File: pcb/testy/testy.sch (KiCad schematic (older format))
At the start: 74 parts, among them J1 Conn_01x02, J2 Conn_01x02, SW0:0 SW_Push, SW0:1 SW_Push, SW0:2 SW_Push, SW0:3 SW_Push, SW0:4 SW_Push, SW0:5 SW_Push, SW1:0 SW_Push, SW1:1 SW_Push, SW1:2 SW_Push, SW1:3 SW_Push, SW1:4 SW_Push, SW1:5 SW_Push, SW2:0 SW_Push, SW2:1 SW_Push, SW2:2 SW_Push, SW2:3 SW_Push, SW2:4 SW_Push, SW2:5 SW_Push, SW3:0 SW_Push, SW3:1 SW_Push, SW3:2 SW_Push, SW3:3 SW_Push, SW3:4 SW_Push, SW3:5 SW_Push, SW3:6 SW_Push, SW4:0 SW_Push, SW4:1 SW_Push, SW4:2 SW_Push, SW4:3 SW_Push, SW4:4 SW_Push, SW4:5 SW_Push, SW4:6 SW_Push, U1 ProMicro

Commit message: feat: attempt to make usb-c breakout board footprint
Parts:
- added H1: USB-C Breakout Board, footprints:usb-c-breakout, symbol Mechanical:MountingHole
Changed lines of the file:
@@
 Wire Wire Line
 	10000 4650 10250 4650
+$Comp
+L Mechanical:MountingHole H1
+U 1 1 5DCB9C3F
+P 1950 7200
+F 0 "H1" H 2050 7246 50  0000 L CNN
+F 1 "USB-C Breakout Board" H 2050 7155 50  0000 L CNN
+F 2 "footprints:usb-c-breakout" H 1950 7200 50  0001 C CNN
+F 3 "~" H 1950 7200 50  0001 C CNN
+	1    1950 7200
+	1    0    0    -1
+$EndComp
 $EndSCHEMATC

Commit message: feat: add OLED and iCSP to schematic
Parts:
- added JP1, JP2, JP3, JP4, JP5, JP6, JP7, JP8: JP2, symbol jp2:JP2
- added P1: OLED, symbol conn_01x04:CONN_01X04
- added P2: iCSP, symbol conn_01x06:CONN_01X06
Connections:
- net labels added: MISO, MOSI, SCK, SCL, SDA
- wire segments 107 -> 148
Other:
- note added: "FIXME add I2C resistors"
- note added: "FIXME add LED resistors"
- note added: "FIXME can I use PD3 pin for driving an LED?\nAlternatively, can I drive 3 LEDs with fewer than 3 pins?"
- note added: "Left hand side"
- note added: "Right hand side"

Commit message: fix: updates related to copying helix underglow
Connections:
- net labels added: LED
- no-connect marks 0 -> 2
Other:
- note added: "FIXME can I use PD3 pin for driving an LED? Yes! Helix does it.\nAlternatively, can I drive 3 LEDs with fewer than 3 pins? Yes, use WS2812\n"
- note added: "FIXME remove separate LEDs and copy helix method of driving LEDs\nHelix D3 pin config means PD3, not D3=PD0"
- note removed: "FIXME can I use PD3 pin for driving an LED?\nAlternatively, can I drive 3 LEDs with fewer than 3 pins?"
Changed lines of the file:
@@
 	1200 5200 1200 5650
 Text GLabel 1250 1900 0    50   Input ~ 0
-LED0
-Text GLabel 1250 3000 0    50   Input ~ 0
-LED1
-Text GLabel 2250 3000 2    50   Input ~ 0
-LED2
+LED
 Text GLabel 2250 4700 2    50   Input ~ 0
 LED0
@@
 SCL
 Text Notes 900  1400 0    50   ~ 0
-FIXME can I use PD3 pin for driving an LED?\nAlternatively, can I drive 3 LEDs with fewer than 3 pins?
+FIXME can I use PD3 pin for driving an LED? Yes! Helix does it.\nAlternatively, can I drive 3 LEDs with fewer than 3 pins? Yes, use WS2812\n
 $Comp
 L conn_01x04:CONN_01X04 P1
@@
 Text Notes 8900 6100 2    50   ~ 0
 FIXME add LED resistors
+NoConn ~ 2250 3000
+NoConn ~ 1250 3000
+Text Notes 2600 5050 0    50   ~ 0
+FIXME remove separate LEDs and copy helix method of driving LEDs\nHelix D3 pin config means PD3, not D3=PD0
 $EndSCHEMATC

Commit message: feat: move to new 5 col version
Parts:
- removed D0:5, D1:5, D2:5, D3:6, D4:0, D4:6: 1N4148, Diode_THT:D_DO-35_SOD27_P7.62mm_Horizontal, symbol Diode:1N4148
- removed H1: USB-C Breakout Board, footprints:usb-c-breakout, symbol Mechanical:MountingHole
- removed J1, J2: Conn_01x02, footprints:edge-connector, symbol Connector_Generic:Conn_01x02
- removed LED0: LED, footprints:LED_D3.0mm, symbol led:LED
- removed LED1, LED2: LED, LED_THT:LED_D3.0mm, symbol led:LED
- removed SW0:5, SW1:5, SW2:5, SW3:6, SW4:0, SW4:6: SW_Push, footprints:kailh-socket-and-choc-solder-reversible, symbol Switch:SW_Push
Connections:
- net labels removed: LED0, LED1, LED2
- wire segments 148 -> 119
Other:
- note added: "FIXME add WSxxxx LED strips\nHelix D3 pin config means PD3, not D3=PD0"
- note removed: "FIXME can I use PD3 pin for driving an LED? Yes! Helix does it.\nAlternatively, can I drive 3 LEDs with fewer than 3 pins? Yes, use WS2812\n"
- note removed: "FIXME remove separate LEDs and copy helix method of driving LEDs\nHelix D3 pin config means PD3, not D3=PD0"

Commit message: feat: lots done, still need more LEDs, the I2C resistors and finish the traces
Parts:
- added LED1: SK6812mini, footprints:ws2812-single, symbol sk6812mini:SK6812mini
- JP1: value JP2 -> L_GND; footprint (none) -> footprints:Jumper
- JP2: value JP2 -> L_VCC; footprint (none) -> footprints:Jumper
- JP3: value JP2 -> L_SCL; footprint (none) -> footprints:Jumper
- JP4: value JP2 -> L_SDA; footprint (none) -> footprints:Jumper
- JP5: value JP2 -> R_SDA; footprint (none) -> footprints:Jumper
- JP6: value JP2 -> R_SCL; footprint (none) -> footprints:Jumper
- JP7: value JP2 -> R_VCC; footprint (none) -> footprints:Jumper
- JP8: value JP2 -> R_GND; footprint (none) -> footprints:Jumper
- P1: footprint (none) -> footprints:oled_header_helix
- P2: footprint (none) -> footprints:PinHeader_1x06_P2.54mm_Vertical
- renumbered U1 to PM1
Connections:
- net GND: now also LED1.2 (GND)
- net LED: now also LED1.3 (DIN)
- net VCC: now also LED1.4 (VDD)
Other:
- note removed: "FIXME add LED resistors"
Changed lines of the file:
@@
 Row2
 $Comp
-L promicro:ProMicro U1
+L promicro:ProMicro PM1
 U 1 1 5DB7A2E7
 P 1750 2250
-F 0 "U1" H 1750 2847 60  0000 C CNN
+F 0 "PM1" H 1750 2847 60  0000 C CNN
 F 1 "ProMicro" H 1750 2741 60  0000 C CNN
 F 2 "footprints:Pro_Micro_ergotravel" H 1750 2250 60  0001 C CNN
@@
 U 1 1 5DCD19CA
 P 4050 5700
-F 0 "P1" H 3967 6065 50  0000 C CNN
+F 0 "P1" H 3967 6065 50  0001 C CNN
 F 1 "OLED" H 3967 5974 50  0000 C CNN
-F 2 "" H 4050 5700 50  0000 C CNN
+F 2 "footprints:oled_header_helix" H 4050 5700 50  0001 C CNN
 F 3 "" H 4050 5700 50  0000 C CNN
 	1    4050 5700
@@
 U 1 1 5DCEEF2E
 P 4950 5400
-F 0 "JP1" V 4837 5400 50  0000 C CNN
-F 1 "JP2" V 4845 5400 40  0001 C CNN
-F 2 "" H 4950 5400 60  0000 C CNN
+F 0 "JP1" V 4837 5400 50  0001 C CNN
+F 1 "L_GND" V 4845 5400 40  0000 C CNN
+F 2 "footprints:Jumper" H 4950 5400 60  0001 C CNN
 F 3 "" H 4950 5400 60  0000 C CNN
 	1    4950 5400
@@
 U 1 1 5DCF00CE
 P 4950 5600
-F 0 "JP2" V 4837 5600 50  0000 C CNN
-F 1 "JP2" V 4845 5600 40  0001 C CNN
-F 2 "" H 4950 5600 60  0000 C CNN
+F 0 "JP2" V 4837 5600 50  0001 C CNN
+F 1 "L_VCC" V 4845 5600 40  0000 C CNN
+F 2 "footprints:Jumper" H 4950 5600 60  0001 C CNN
 F 3 "" H 4950 5600 60  0000 C CNN
 	1    4950 5600
@@
 U 1 1 5DCF0797
 P 4950 6000
-F 0 "JP4" V 4837 6000 50  0000 C CNN
-F 1 "JP2" V 4845 6000 40  0001 C CNN
-F 2 "" H 4950 6000 60  0000 C CNN
+F 0 "JP4" V 4837 6000 50  0001 C CNN
+F 1 "L_SDA" V 4845 6000 40  0000 C CNN
+F 2 "footprints:Jumper" H 4950 6000 60  0001 C CNN
 F 3 "" H 4950 6000 60  0000 C CNN
 	1    4950 6000
@@
 U 1 1 5DCF0E97
 P 4950 5800
-F 0 "JP3" V 4837 5800 50  0000 C CNN
-F 1 "JP2" V 4845 5800 40  0001 C CNN
-F 2 "" H 4950 5800 60  0000 C CNN
+F 0 "JP3" V 4837 5800 50  0001 C CNN
+F 1 "L_SCL" V 4845 5800 40  0000 C CNN
+F 2 "footprints:Jumper" H 4950 5800 60  0001 C CNN
 F 3 "" H 4950 5800 60  0000 C CNN
 	1    4950 5800
@@
 $EndComp
 $Comp
-L power:VCC #PWR?
+L power:VCC #PWR0106
 U 1 1 5DCFEAE0
 P 5500 5600
-F 0 "#PWR?" H 5500 5450 50  0001 C CNN
+F 0 "#PWR0106" H 5500 5450 50  0001 C CNN
 F 1 "VCC" H 5517 5773 50  0000 C CNN
 F 2 "" H 5500 5600 50  0001 C CNN
@@
 $EndComp
 $Comp
-L power:GND #PWR?
+L power:GND #PWR0107
 U 1 1 5DD07F88
 P 5500 5400
-F 0 "#PWR?" H 5500 5150 50  0001 C CNN
+F 0 "#PWR0107" H 5500 5150 50  0001 C CNN
 F 1 "GND" H 5505 5227 50  0000 C CNN
 F 2 "" H 5500 5400 50  0001 C CNN
@@
 U 1 1 5DD6CDF9
 P 4950 7000
-F 0 "JP8" V 5063 7000 50  0000 C CNN
-F 1 "JP2" V 4845 7000 40  0001 C CNN
-F 2 "" H 4950 7000 60  0000 C CNN
+F 0 "JP8" V 5063 7000 50  0001 C CNN
+F 1 "R_GND" V 4845 7000 40  0000 C CNN
+F 2 "footprints:Jumper" H 4950 7000 60  0001 C CNN
 F 3 "" H 4950 7000 60  0000 C CNN
 	1    4950 7000
@@
 U 1 1 5DD6CE03
 P 4950 6800
-F 0 "JP7" V 5063 6800 50  0000 C CNN
-F 1 "JP2" V 4845 6800 40  0001 C CNN
-F 2 "" H 4950 6800 60  0000 C CNN
+F 0 "JP7" V 5063 6800 50  0001 C CNN
+F 1 "R_VCC" V 4845 6800 40  0000 C CNN
+F 2 "footprints:Jumper" H 4950 6800 60  0001 C CNN
 F 3 "" H 4950 6800 60  0000 C CNN
 	1    4950 6800
@@
 U 1 1 5DD6CE0D
 P 4950 6400
-F 0 "JP5" V 5063 6400 50  0000 C CNN
-F 1 "JP2" V 4845 6400 40  0001 C CNN
-F 2 "" H 4950 6400 60  0000 C CNN
+F 0 "JP5" V 5063 6400 50  0001 C CNN
+F 1 "R_SDA" V 4845 6400 40  0000 C CNN
+F 2 "footprints:Jumper" H 4950 6400 60  0001 C CNN
 F 3 "" H 4950 6400 60  0000 C CNN
 	1    4950 6400
@@
 U 1 1 5DD6CE17
 P 4950 6600
-F 0 "JP6" V 5063 6600 50  0000 C CNN
-F 1 "JP2" V 4845 6600 40  0001 C CNN
-F 2 "" H 4950 6600 60  0000 C CNN
+F 0 "JP6" V 5063 6600 50  0001 C CNN
+F 1 "R_SCL" V 4845 6600 40  0000 C CNN
+F 2 "footprints:Jumper" H 4950 6600 60  0001 C CNN
 F 3 "" H 4950 6600 60  0000 C CNN
 	1    4950 6600
@@
 Right hand side
 $Comp
-L power:VCC #PWR?
+L power:VCC #PWR0108
 U 1 1 5DD6CE22
 P 5500 6800
-F 0 "#PWR?" H 5500 6650 50  0001 C CNN
+F 0 "#PWR0108" H 5500 6650 50  0001 C CNN
 F 1 "VCC" H 5517 6973 50  0000 C CNN
 F 2 "" H 5500 6800 50  0001 C CNN
@@
 $EndComp
 $Comp
-L power:GND #PWR?
+L power:GND #PWR0109
 U 1 1 5DD6CE2C
 P 5500 7000
-F 0 "#PWR?" H 5500 6750 50  0001 C CNN
+F 0 "#PWR0109" H 5500 6750 50  0001 C CNN
 F 1 "GND" H 5505 6827 50  0000 C CNN
 F 2 "" H 5500 7000 50  0001 C CNN
@@
 F 0 "P2" H 6467 6215 50  0000 C CNN
 F 1 "iCSP" H 6467 6124 50  0000 C CNN
-F 2 "" H 6550 5750 50  0000 C CNN
+F 2 "footprints:PinHeader_1x06_P2.54mm_Vertical" H 6550 5750 50  0001 C CNN
 F 3 "" H 6550 5750 50  0000 C CNN
 	1    6550 5750
@@
 $EndComp
 $Comp
-L power:VCC #PWR?
+L power:VCC #PWR0110
 U 1 1 5DDE0229
 P 7000 5600
-F 0 "#PWR?" H 7000 5450 50  0001 C CNN
+F 0 "#PWR0110" H 7000 5450 50  0001 C CNN
 F 1 "VCC" H 7017 5773 50  0000 C CNN
 F 2 "" H 7000 5600 50  0001 C CNN
@@
 $EndComp
 $Comp
-L power:GND #PWR?
+L power:GND #PWR0111
 U 1 1 5DDE0C00
 P 7000 6000
-F 0 "#PWR?" H 7000 5750 50  0001 C CNN
+F 0 "#PWR0111" H 7000 5750 50  0001 C CNN
 F 1 "GND" H 7005 5827 50  0000 C CNN
 F 2 "" H 7000 6000 50  0001 C CNN
@@
 Wire Wire Line
 	2550 2650 2550 2550
-Text Notes 8900 5750 2    50   ~ 0
+Text Notes 9050 5700 2    50   ~ 0
 FIXME add I2C resistors
-Text Notes 8900 6100 2    50   ~ 0
-FIXME add LED resistors
 NoConn ~ 2250 3000
 NoConn ~ 1250 3000
-Text Notes 1250 5200 0    50   ~ 0
+Text Notes 1000 5100 0    50   ~ 0
 FIXME add WSxxxx LED strips\nHelix D3 pin config means PD3, not D3=PD0
 Connection ~ 5650 4650
@@
 Wire Wire Line
 	3650 4650 5650 4650
+$Comp
+L sk6812mini:SK6812mini LED1
+U 1 1 5DE1DE41
+P 1700 5500
+F 0 "LED1" H 2044 5500 60  0000 L CNN
+F 1 "SK6812mini" H 2044 5447 39  0001 L CNN
+F 2 "footprints:ws2812-single" H 2044 5447 60  0001 L CNN
+F 3 "" H 1700 5500 60  0000 C CNN
+	1    1700 5500
+	1    0    0    -1
+$EndComp
+$Comp
+L power:GND #PWR0112
+U 1 1 5DE1F507
+P 1600 5800
+F 0 "#PWR0112" H 1600 5550 50  0001 C CNN
+F 1 "GND" H 1605 5627 50  0000 C CNN
+F 2 "" H 1600 5800 50  0001 C CNN
+F 3 "" H 1600 5800 50  0001 C CNN
+	1    1600 5800
+	1    0    0    -1
+$EndComp
+$Comp
+L power:VCC #PWR0113
+U 1 1 5DE241AF
+P 1800 5200
+F 0 "#PWR0113" H 1800 5050 50  0001 C CNN
+F 1 "VCC" H 1818 5373 50  0000 C CNN
+F 2 "" H 1800 5200 50  0001 C CNN
+F 3 "" H 1800 5200 50  0001 C CNN
+	1    1800 5200
+	0    1    1    0
+$EndComp
+Text GLabel 2000 5600 2    50   Input ~ 0
+LED
 $EndSCHEMATC

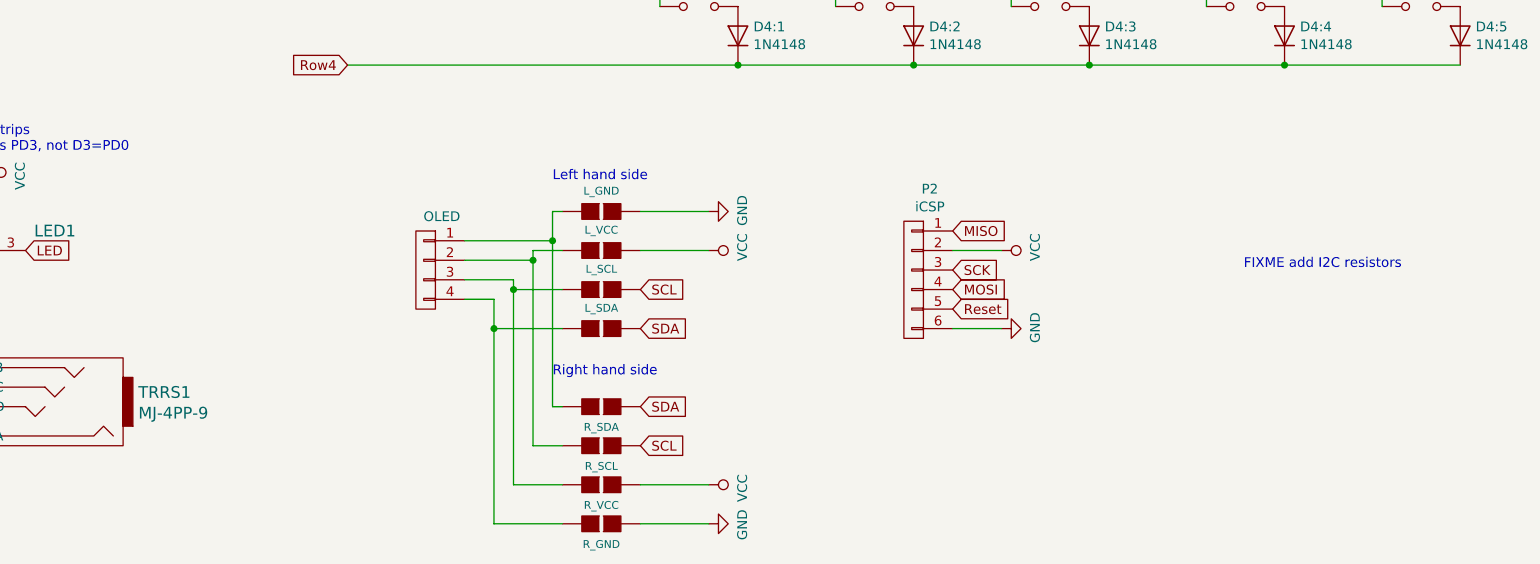
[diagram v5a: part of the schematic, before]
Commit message: feat: fully wired but stuff one side of the oled panels
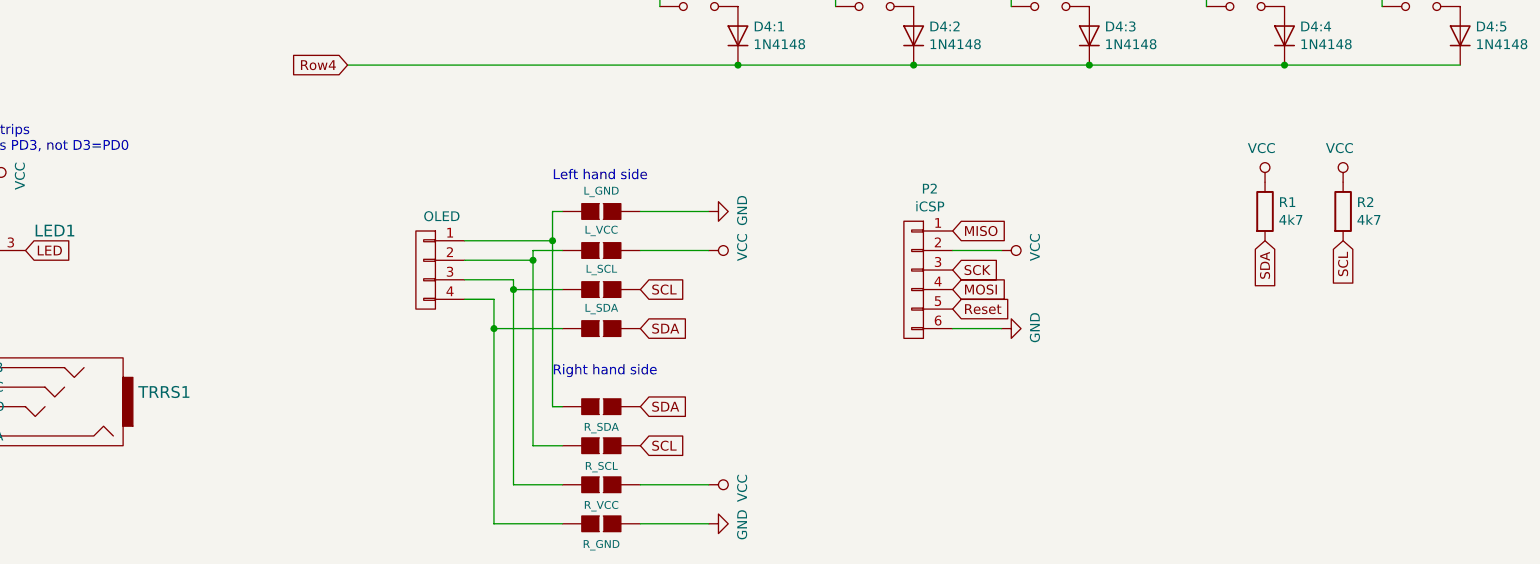
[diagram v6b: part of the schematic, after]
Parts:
- added R1, R2: 4k7, footprints:resistor, symbol resistor:R
- TRRS1: footprint footprints:TRRS-PJ-320A-dual -> footprints:TRRS-helix
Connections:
- net SCL: now also R2.2
- net SDA: now also R1.2
- net VCC: now also R1.1, R2.1
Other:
- note removed: "FIXME add I2C resistors"
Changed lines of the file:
@@
 P 2100 6400
 F 0 "TRRS1" H 1622 6327 60  0000 R CNN
-F 1 "MJ-4PP-9" H 1622 6433 60  0000 R CNN
-F 2 "footprints:TRRS-PJ-320A-dual" H 2050 6650 60  0001 C CNN
+F 1 "MJ-4PP-9" H 1622 6433 60  0001 R CNN
+F 2 "footprints:TRRS-helix" H 2050 6650 60  0001 C CNN
 F 3 "" H 2100 6400 60  0000 C CNN
 	1    2100 6400
@@
 Wire Wire Line
 	2550 2650 2550 2550
-Text Notes 9050 5700 2    50   ~ 0
-FIXME add I2C resistors
 NoConn ~ 2250 3000
 NoConn ~ 1250 3000
@@
 Text GLabel 2000 5600 2    50   Input ~ 0
 LED
+$Comp
+L resistor:R R1
+U 1 1 5DE28F05
+P 8350 5400
+F 0 "R1" H 8420 5446 50  0000 L CNN
+F 1 "4k7" H 8420 5355 50  0000 L CNN
+F 2 "footprints:resistor" H 8420 5309 50  0001 L CNN
+F 3 "" H 8350 5400 50  0000 C CNN
+	1    8350 5400
+	1    0    0    -1
+$EndComp
+$Comp
+L resistor:R R2
+U 1 1 5DE296C1
+P 8750 5400
+F 0 "R2" H 8820 5446 50  0000 L CNN
+F 1 "4k7" H 8820 5355 50  0000 L CNN
+F 2 "footprints:resistor" H 8820 5309 50  0001 L CNN
+F 3 "" H 8750 5400 50  0000 C CNN
+	1    8750 5400
+	1    0    0    -1
+$EndComp
+$Comp
+L power:VCC #PWR?
+U 1 1 5DE2DAE3
+P 8750 5250
+F 0 "#PWR?" H 8750 5100 50  0001 C CNN
+F 1 "VCC" H 8767 5423 50  0000 C CNN
+F 2 "" H 8750 5250 50  0001 C CNN
+F 3 "" H 8750 5250 50  0001 C CNN
+	1    8750 5250
+	-1   0    0    -1
+$EndComp
+$Comp
+L power:VCC #PWR?
+U 1 1 5DE2E515
+P 8350 5250
+F 0 "#PWR?" H 8350 5100 50  0001 C CNN
+F 1 "VCC" H 8367 5423 50  0000 C CNN
+F 2 "" H 8350 5250 50  0001 C CNN
+F 3 "" H 8350 5250 50  0001 C CNN
+	1    8350 5250
+	-1   0    0    -1
+$EndComp
+Text GLabel 8750 5550 3    50   Input ~ 0
+SCL
+Text GLabel 8350 5550 3    50   Input ~ 0
+SDA
 $EndSCHEMATC

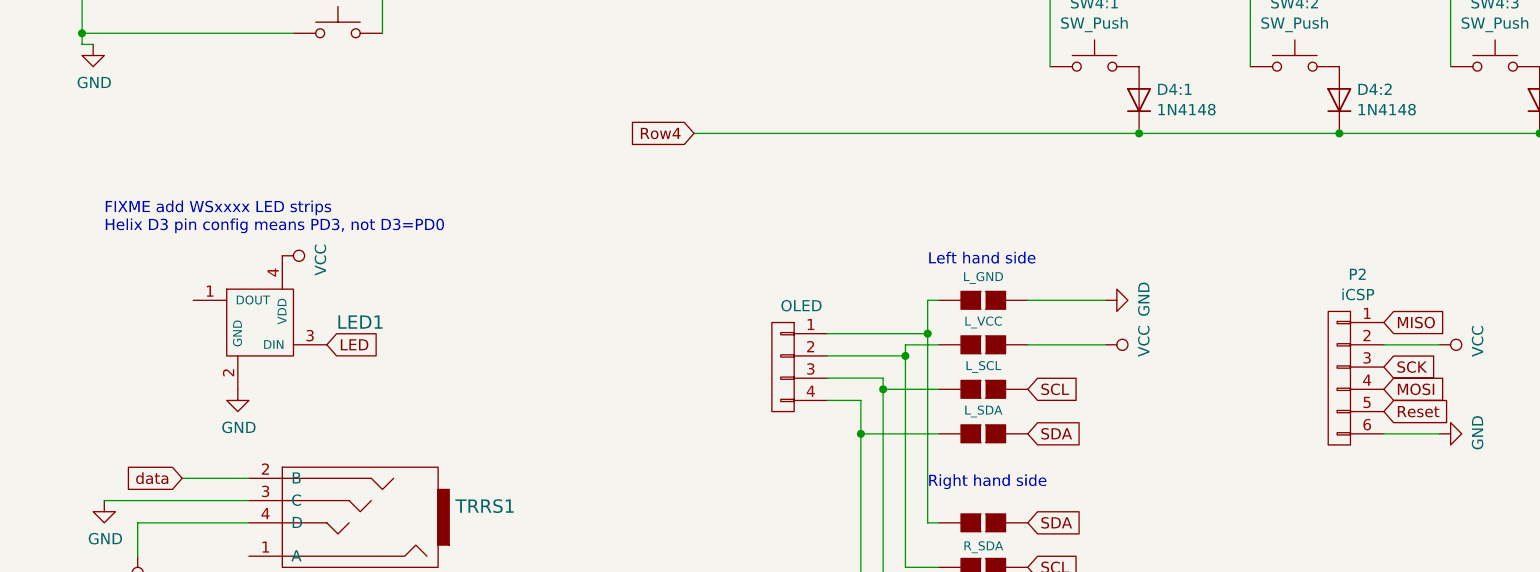
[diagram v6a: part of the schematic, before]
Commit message: feat: fill in zones, add instructions, correct OLED jumpers on right(bottom), still need to finalise LED wiring
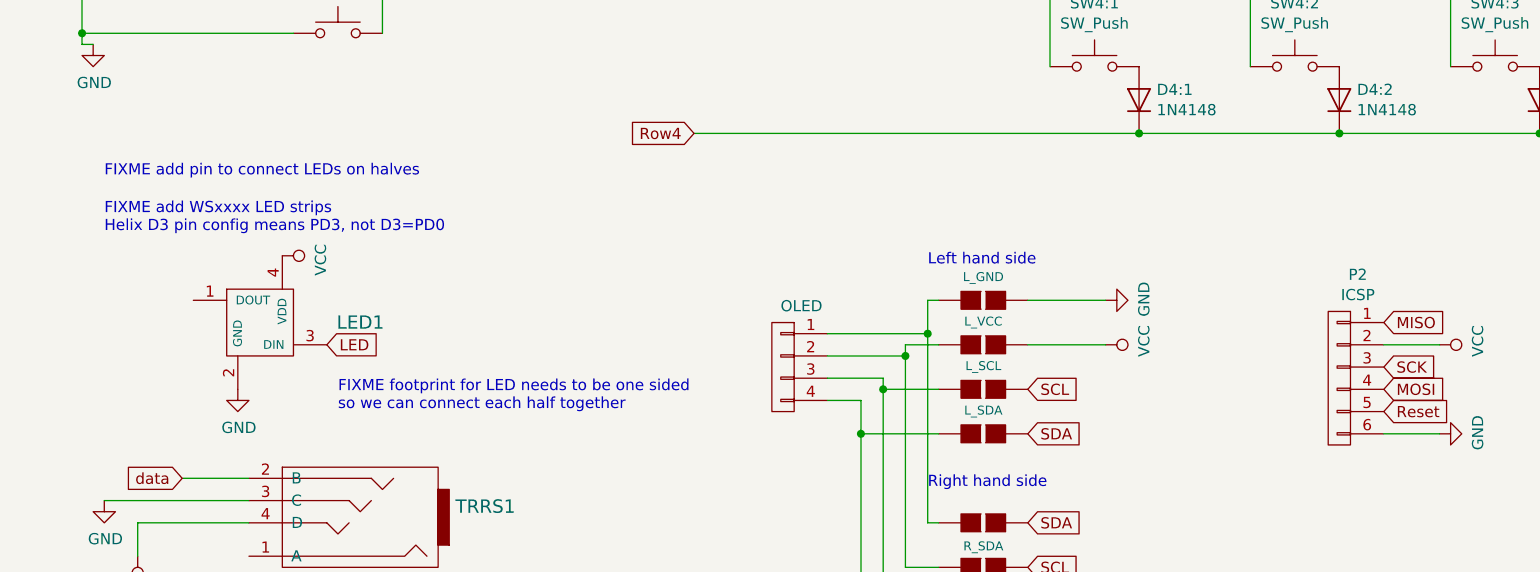
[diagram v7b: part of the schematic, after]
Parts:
- P2: value iCSP -> ICSP
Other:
- note added: "FIXME add pin to connect LEDs on halves"
- note added: "FIXME footprint for LED needs to be one sided\nso we can connect each half together"
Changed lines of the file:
@@
 P 6550 5750
 F 0 "P2" H 6467 6215 50  0000 C CNN
-F 1 "iCSP" H 6467 6124 50  0000 C CNN
+F 1 "ICSP" H 6467 6124 50  0000 C CNN
 F 2 "footprints:PinHeader_1x06_P2.54mm_Vertical" H 6550 5750 50  0001 C CNN
 F 3 "" H 6550 5750 50  0000 C CNN
@@
 $EndComp
 $Comp
-L power:VCC #PWR?
+L power:VCC #PWR0114
 U 1 1 5DE2DAE3
 P 8750 5250
-F 0 "#PWR?" H 8750 5100 50  0001 C CNN
+F 0 "#PWR0114" H 8750 5100 50  0001 C CNN
 F 1 "VCC" H 8767 5423 50  0000 C CNN
 F 2 "" H 8750 5250 50  0001 C CNN
@@
 $EndComp
 $Comp
-L power:VCC #PWR?
+L power:VCC #PWR0115
 U 1 1 5DE2E515
 P 8350 5250
-F 0 "#PWR?" H 8350 5100 50  0001 C CNN
+F 0 "#PWR0115" H 8350 5100 50  0001 C CNN
 F 1 "VCC" H 8367 5423 50  0000 C CNN
 F 2 "" H 8350 5250 50  0001 C CNN
@@
 Text GLabel 8350 5550 3    50   Input ~ 0
 SDA
+Text Notes 1000 4850 0    50   ~ 0
+FIXME add pin to connect LEDs on halves
+Text Notes 2050 5900 0    50   ~ 0
+FIXME footprint for LED needs to be one sided\nso we can connect each half together
 $EndSCHEMATC
